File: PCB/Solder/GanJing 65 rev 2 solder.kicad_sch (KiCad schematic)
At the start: 149 parts, among them SW1 EC11_rotary_encoder, U1 Elite-C

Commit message: Updating soldered version
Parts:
- removed MX75: MX_ISO_no_LED_flipped_stabs, GanJing_components:MX_ISO_no_LED_flipped_stabs, symbol GanJing_components:MX_ISO_no_LED_flipped_stabs
- added D59, D64, D65, D67: 1N4148TR_diode, GanJing_components:1N4148TR_diode, symbol GanJing_components:1N4148TR_diode
- added MX59: MX_1u_no_LED, GanJing_components:MX_1u_no_LED, symbol GanJing_components:MX_1u_no_LED
- added MX76: MX_ISO_no_LED_flipped_stabs, GanJing_components:MX_ISO_no_LED_flipped_stabs, symbol GanJing_components:MX_ISO_no_LED_flipped_stabs
- added MX78: MX_1.75u_no_LED, GanJing_components:MX_1.75u_no_LED, symbol GanJing_components:MX_1.75u_no_LED
- MX44: renamed from MX43; footprint GanJing_components:MX_2.25u_no_LED -> GanJing_components:MX_2.25u_no_LED_flipped_stabs
- renumbered D70 to D15, D15 to D16, D16 to D17, D17 to D18, D18 to D19, D19 to D20, D20 to D21, D21 to D22, D22 to D23, D23 to D24, D24 to D25, D25 to D26, D26 to D27, D27 to D28, D28 to D29, D29 to D30, D30 to D31, D31 to D32, D32 to D33, D33 to D34, D34 to D35, D35 to D36, D36 to D37, D37 to D38, D38 to D39, D39 to D40, D40 to D41, D41 to D42, D42 to D43, D43 to D44, D44 to D45, D45 to D46, D46 to D47, D47 to D48, D48 to D49, D49 to D50, D50 to D51, D51 to D52, D52 to D53, D53 to D54, D54 to D55, D55 to D56, D56 to D57, D57 to D58, D58 to D60, D59 to D61, D60 to D62, D61 to D63, D62 to D66, D63 to D68, D64 to D69, D65 to D70, D66 to D71, D67 to D72, D68 to D73, D69 to D74, MX76 to MX15, MX15 to MX16, MX16 to MX17, MX17 to MX18, MX18 to MX19, MX19 to MX20, MX20 to MX21, MX21 to MX22, MX22 to MX23, MX23 to MX24, MX24 to MX25, MX25 to MX26, MX26 to MX27, MX27 to MX28, MX28 to MX29, MX29 to MX30, MX30 to MX31, MX31 to MX32, MX32 to MX33, MX33 to MX34, MX34 to MX35, MX35 to MX36, MX36 to MX37, MX37 to MX38, MX38 to MX39, MX39 to MX40, MX40 to MX41, MX41 to MX42, MX42 to MX43, MX44 to MX45, MX45 to MX46, MX46 to MX47, MX47 to MX48, MX48 to MX49, MX49 to MX50, MX50 to MX51, MX51 to MX52, MX52 to MX53, MX53 to MX54, MX54 to MX55, MX55 to MX56, MX56 to MX57, MX57 to MX58, MX58 to MX60, MX59 to MX61, MX60 to MX62, MX61 to MX63, MX72 to MX64, MX73 to MX65, MX62 to MX66, MX74 to MX67, MX63 to MX68, MX64 to MX69, MX65 to MX70, MX66 to MX71, MX67 to MX72, MX68 to MX73, MX69 to MX74, MX70 to MX75, MX71 to MX77
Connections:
- net col_13: now also MX78.1 (COL)
- net col_14: now also MX59.1 (COL), MX76.1 (COL)
- net col_5: now also MX64.1 (COL)
- net col_6: now also MX65.1 (COL)
- net col_7: no longer MX64.1 (COL), MX65.1 (COL), MX67.1 (COL)
- net col_8: now also MX67.1 (COL)
- net row_4: now also D59.1
- net row_5: now also D64.1, D65.1, D67.1
- net at D44.2, MX44.2 (ROW): now also MX76.2 (ROW)
- net at D58.2, MX58.2 (ROW): now also MX78.2 (ROW)
- net S1 renamed col_15
- new net: D66.2, MX66.2 (ROW)
- new net: D65.2, MX65.2 (ROW)
- new net: D64.2, MX64.2 (ROW)
- new net: D67.2, MX67.2 (ROW)
- new net: D59.2, MX59.2 (ROW)
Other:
- moved on the sheet: D1, D10, D11, D12, D13, D14, D15, D16, D17, D18, D19, D2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

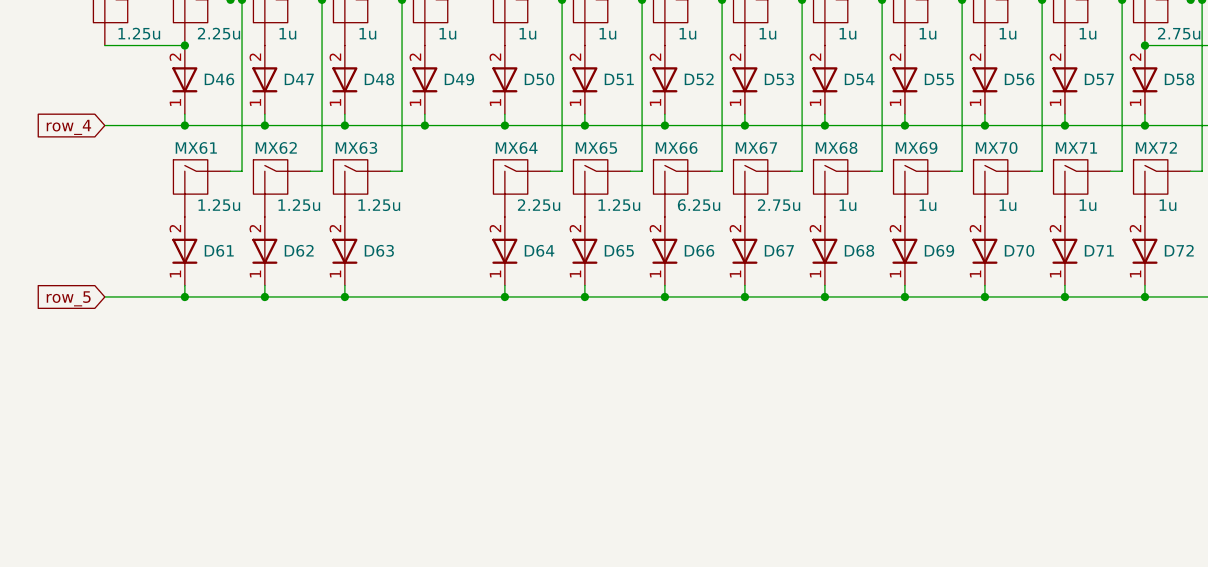
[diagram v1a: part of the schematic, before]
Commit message: Adding 7u to soldered PCB
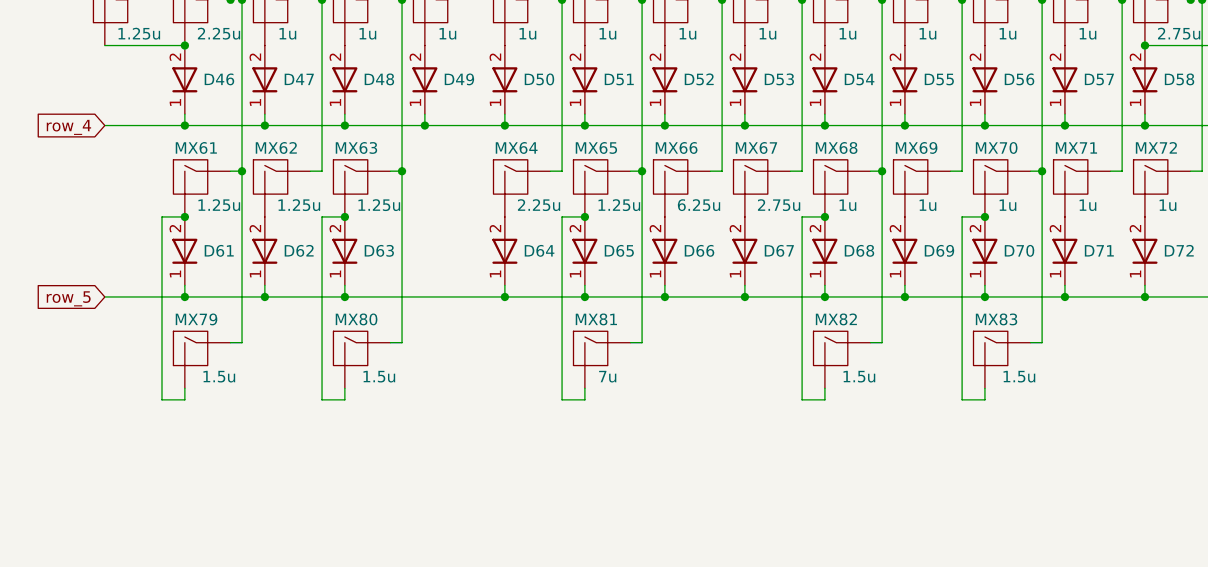
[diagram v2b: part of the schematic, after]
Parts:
- added MX79, MX80, MX82, MX83: MX_1.5u_no_LED, GanJing_components:MX_1.5u_no_LED, symbol GanJing_components:MX_1.5u_no_LED
- added MX81: MX_7u_no_LED_flipped_stabs, GanJing_components:MX_7u_no_LED_flipped_stabs, symbol GanJing_components:MX_7u_no_LED_flipped_stabs
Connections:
- net col_1: now also MX79.1 (COL)
- net col_11: now also MX83.1 (COL)
- net col_3: now also MX80.1 (COL)
- net col_6: now also MX81.1 (COL)
- net col_9: now also MX82.1 (COL)
- net at D61.2, MX61.2 (ROW): now also MX79.2 (ROW)
- net at D63.2, MX63.2 (ROW): now also MX80.2 (ROW)
- net at D65.2, MX65.2 (ROW): now also MX81.2 (ROW)
- net at D68.2, MX68.2 (ROW): now also MX82.2 (ROW)
- net at D70.2, MX70.2 (ROW): now also MX83.2 (ROW)
